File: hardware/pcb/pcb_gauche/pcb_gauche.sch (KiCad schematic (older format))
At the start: 18 parts, among them P1 TE-FFC-10-0.5

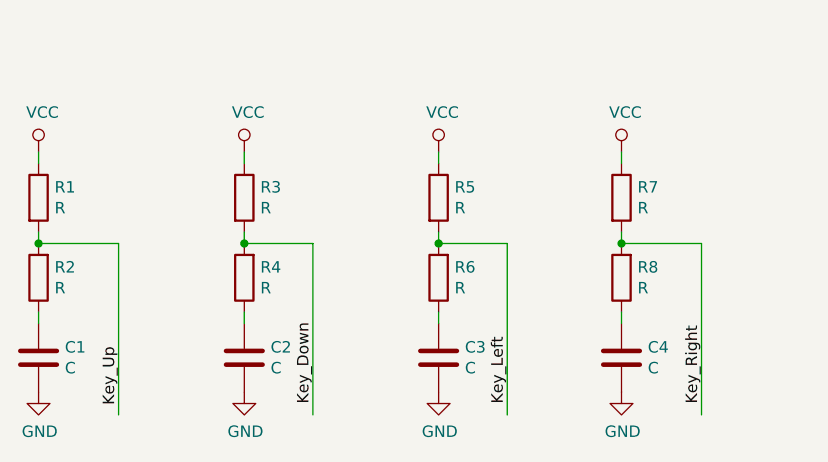
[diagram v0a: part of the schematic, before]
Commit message: Modifications des fonts et debut de la creation du drivers de touches
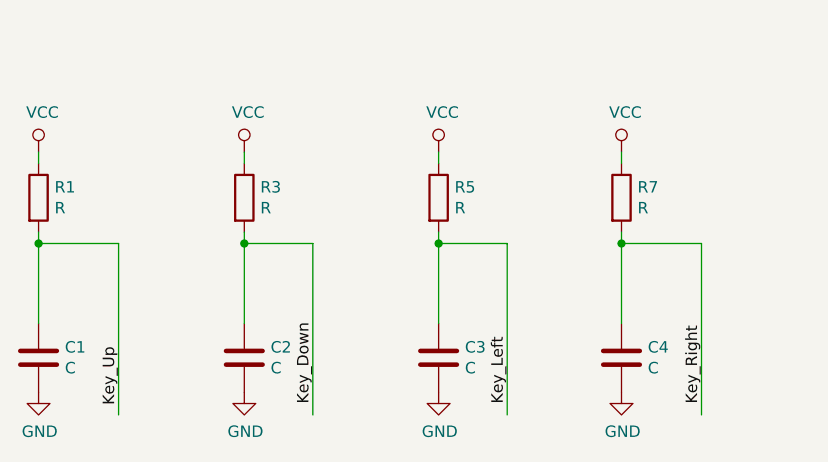
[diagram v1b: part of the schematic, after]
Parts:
- removed R2, R4, R6, R8: R, Resistor_SMD:R_1206_3216Metric_Pad1.42x1.75mm_HandSolder, symbol Device:R
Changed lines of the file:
@@
-$EndComp
-$Comp
-L Device:R R2
-U 1 1 5C793610
-P 1950 5750
-F 0 "R2" H 1880 5704 50  0000 R CNN
-F 1 "R" H 1880 5795 50  0000 R CNN
-F 2 "Resistor_SMD:R_1206_3216Metric_Pad1.42x1.75mm_HandSolder" V 1880 5750 50  0001 C CNN
-F 3 "~" H 1950 5750 50  0001 C CNN
-	1    1950 5750
-	-1   0    0    1
 $EndComp
 $Comp
@@
 $EndComp
 Wire Wire Line
-	1950 5900 1950 5950
-Wire Wire Line
 	1950 5550 1950 5600
 $Comp
@@
 $EndComp
 $Comp
-L Device:R R4
-U 1 1 5C795C8C
-P 2850 5750
-F 0 "R4" H 2780 5704 50  0000 R CNN
-F 1 "R" H 2780 5795 50  0000 R CNN
-F 2 "Resistor_SMD:R_1206_3216Metric_Pad1.42x1.75mm_HandSolder" V 2780 5750 50  0001 C CNN
-F 3 "~" H 2850 5750 50  0001 C CNN
-	1    2850 5750
-	-1   0    0    1
-$EndComp
-$Comp
 L power:GND #PWR0105
 U 1 1 5C795C93
@@
 $EndComp
 Wire Wire Line
-	2850 5900 2850 5950
-Wire Wire Line
 	2850 5550 2850 5600
 $Comp
@@
 $EndComp
 $Comp
-L Device:R R6
-U 1 1 5C79623C
-P 3700 5750
-F 0 "R6" H 3630 5704 50  0000 R CNN
-F 1 "R" H 3630 5795 50  0000 R CNN
-F 2 "Resistor_SMD:R_1206_3216Metric_Pad1.42x1.75mm_HandSolder" V 3630 5750 50  0001 C CNN
-F 3 "~" H 3700 5750 50  0001 C CNN
-	1    3700 5750
-	-1   0    0    1
-$EndComp
-$Comp
 L power:GND #PWR0107
 U 1 1 5C796243
@@
 $EndComp
 Wire Wire Line
-	3700 5900 3700 5950
-Wire Wire Line
 	3700 5550 3700 5600
 $Comp
@@
 $EndComp
 $Comp
-L Device:R R8
-U 1 1 5C79684A
-P 4500 5750
-F 0 "R8" H 4430 5704 50  0000 R CNN
-F 1 "R" H 4430 5795 50  0000 R CNN
-F 2 "Resistor_SMD:R_1206_3216Metric_Pad1.42x1.75mm_HandSolder" V 4430 5750 50  0001 C CNN
-F 3 "~" H 4500 5750 50  0001 C CNN
-	1    4500 5750
-	-1   0    0    1
-$EndComp
-$Comp
 L power:GND #PWR0109
 U 1 1 5C796851
@@
 	1    0    0    -1
 $EndComp
-Wire Wire Line
-	4500 5900 4500 5950
 Wire Wire Line
 	4500 5550 4500 5600
@@
 Wire Wire Line
 	2300 5600 2300 6350
-Connection ~ 1950 5600
 Wire Wire Line
 	2850 5600 3150 5600
 Wire Wire Line
 	3150 5600 3150 6350
-Connection ~ 2850 5600
 Wire Wire Line
 	3700 5600 4000 5600
 Wire Wire Line
 	4000 5600 4000 6350
-Connection ~ 3700 5600
 Wire Wire Line
 	4500 5600 4850 5600
 Wire Wire Line
 	4850 5600 4850 6350
-Connection ~ 4500 5600
 Text Label 2300 6050 3    50   ~ 0
 Key_Up
@@
 Text Label 6800 2050 0    50   ~ 0
 Audio_Left_2
+Wire Wire Line
+	4500 5600 4500 5950
+Connection ~ 4500 5600
+Wire Wire Line
+	3700 5600 3700 5950
+Connection ~ 3700 5600
+Wire Wire Line
+	2850 5600 2850 5950
+Connection ~ 2850 5600
+Wire Wire Line
+	1950 5600 1950 5950
+Connection ~ 1950 5600
 $EndSCHEMATC

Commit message: mise a jour des pcb et design mecaniques
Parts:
- added Logo1: LOGO, Insa:insa-image, symbol insa-sym:LOGO
- SW_DOWN1, SW_LEFT1, SW_RIGHT1, SW_UP1: footprint Button_Switch_THT:SW_PUSH_6mm -> Insa:RubberKey-4mm-2
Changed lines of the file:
@@
 encoding utf-8
 Sheet 1 1
-Title ""
-Date ""
-Rev ""
-Comp ""
+Title "Left side keys PCB"
+Date "2019-04-25"
+Rev "02A"
+Comp "INSA - Toulouse"
 Comment1 ""
 Comment2 ""
@@
 F 0 "SW_UP1" H 3050 2035 50  0000 C CNN
 F 1 "SW_Push" H 3050 1944 50  0000 C CNN
-F 2 "Button_Switch_THT:SW_PUSH_6mm" H 3050 1950 50  0001 C CNN
+F 2 "Insa:RubberKey-4mm-2" H 3050 1950 50  0001 C CNN
 F 3 "~" H 3050 1950 50  0001 C CNN
 	1    3050 1750
@@
 F 0 "SW_RIGHT1" H 3650 2435 50  0000 C CNN
 F 1 "SW_Push" H 3650 2344 50  0000 C CNN
-F 2 "Button_Switch_THT:SW_PUSH_6mm" H 3650 2350 50  0001 C CNN
+F 2 "Insa:RubberKey-4mm-2" H 3650 2350 50  0001 C CNN
 F 3 "~" H 3650 2350 50  0001 C CNN
 	1    3650 2150
@@
 F 0 "SW_LEFT1" H 2600 2435 50  0000 C CNN
 F 1 "SW_Push" H 2600 2344 50  0000 C CNN
-F 2 "Button_Switch_THT:SW_PUSH_6mm" H 2600 2350 50  0001 C CNN
+F 2 "Insa:RubberKey-4mm-2" H 2600 2350 50  0001 C CNN
 F 3 "~" H 2600 2350 50  0001 C CNN
 	1    2600 2150
@@
 F 0 "SW_DOWN1" H 3050 2835 50  0000 C CNN
 F 1 "SW_Push" H 3050 2744 50  0000 C CNN
-F 2 "Button_Switch_THT:SW_PUSH_6mm" H 3050 2750 50  0001 C CNN
+F 2 "Insa:RubberKey-4mm-2" H 3050 2750 50  0001 C CNN
 F 3 "~" H 3050 2750 50  0001 C CNN
 	1    3050 2550
@@
 	1950 5600 1950 5950
 Connection ~ 1950 5600
+$Comp
+L insa-sym:LOGO Logo1
+U 1 1 5CC16F2E
+P 7600 6800
+F 0 "Logo1" H 7600 6348 60  0001 C CNN
+F 1 "LOGO" H 7600 7252 60  0001 C CNN
+F 2 "Insa:insa-image" H 7600 6800 50  0001 C CNN
+F 3 "" H 7600 6800 50  0001 C CNN
+	1    7600 6800
+	1    0    0    -1
+$EndComp
 $EndSCHEMATC
